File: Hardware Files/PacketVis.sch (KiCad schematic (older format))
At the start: 36 parts, among them J1 USB_B_Micro, J2 Conn_01x04, SW1 SW_Push_Dual, SW2 SW_SPST, SW3 SW_SPST, U1 3.3V 1A, U2 74HC595, U3 ESP-WROOM-02D

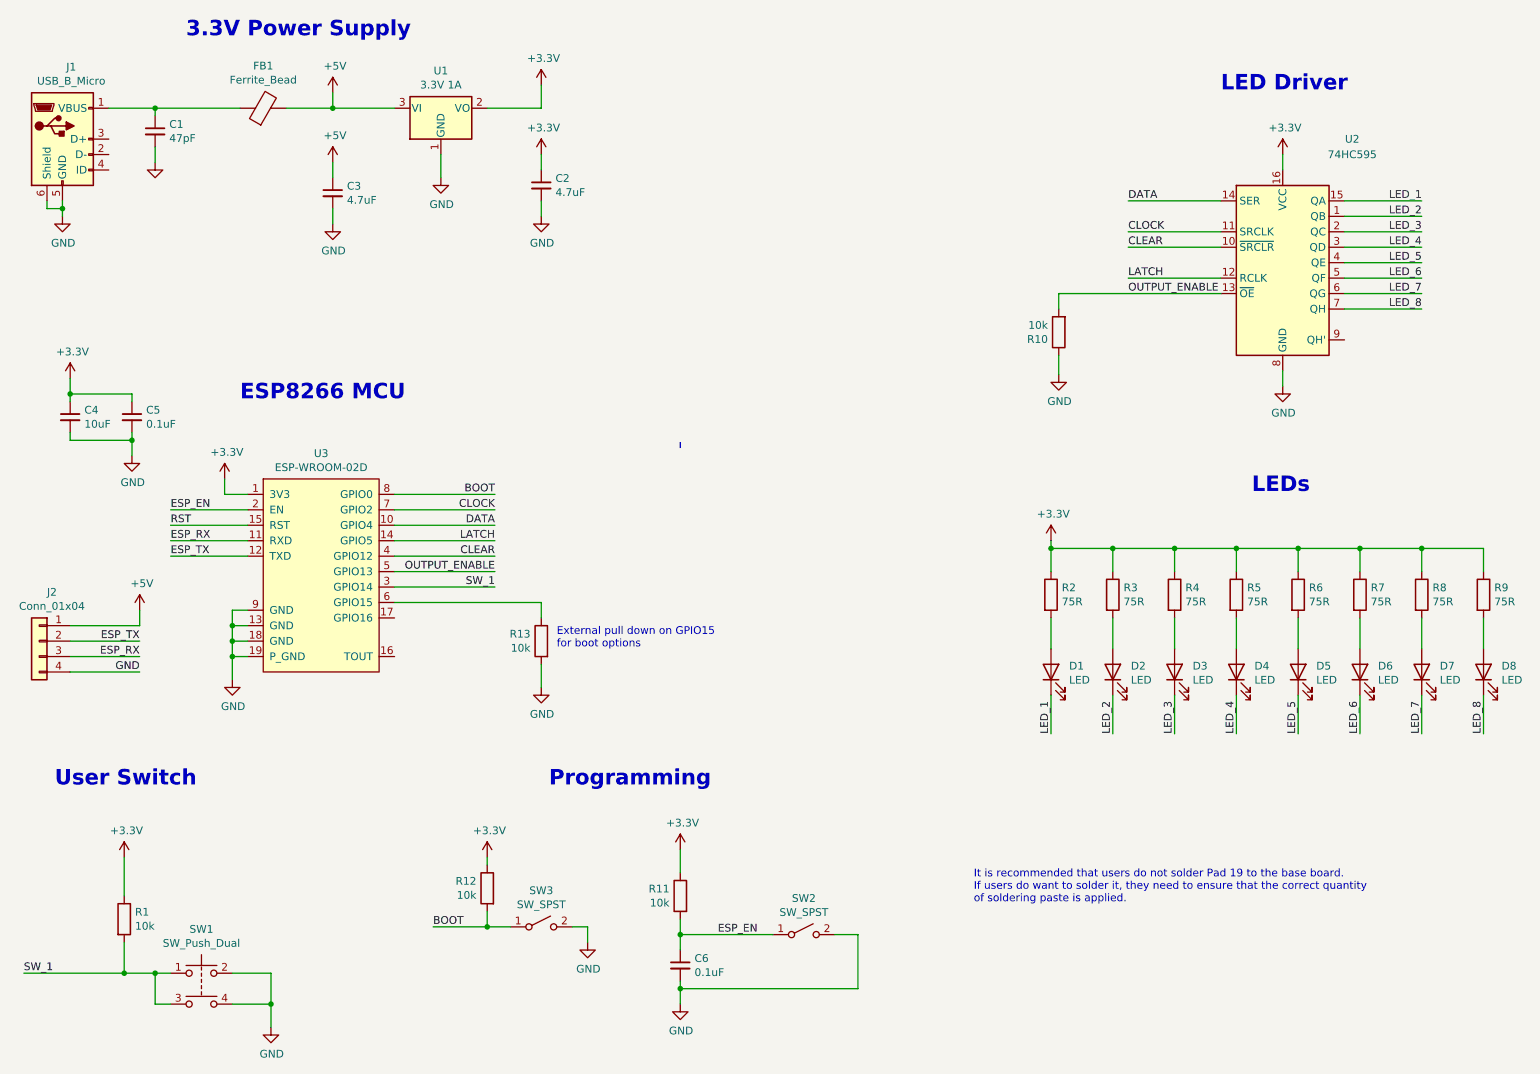
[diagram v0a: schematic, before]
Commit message: Change LEDs to source current from shift register, unroute most tracks
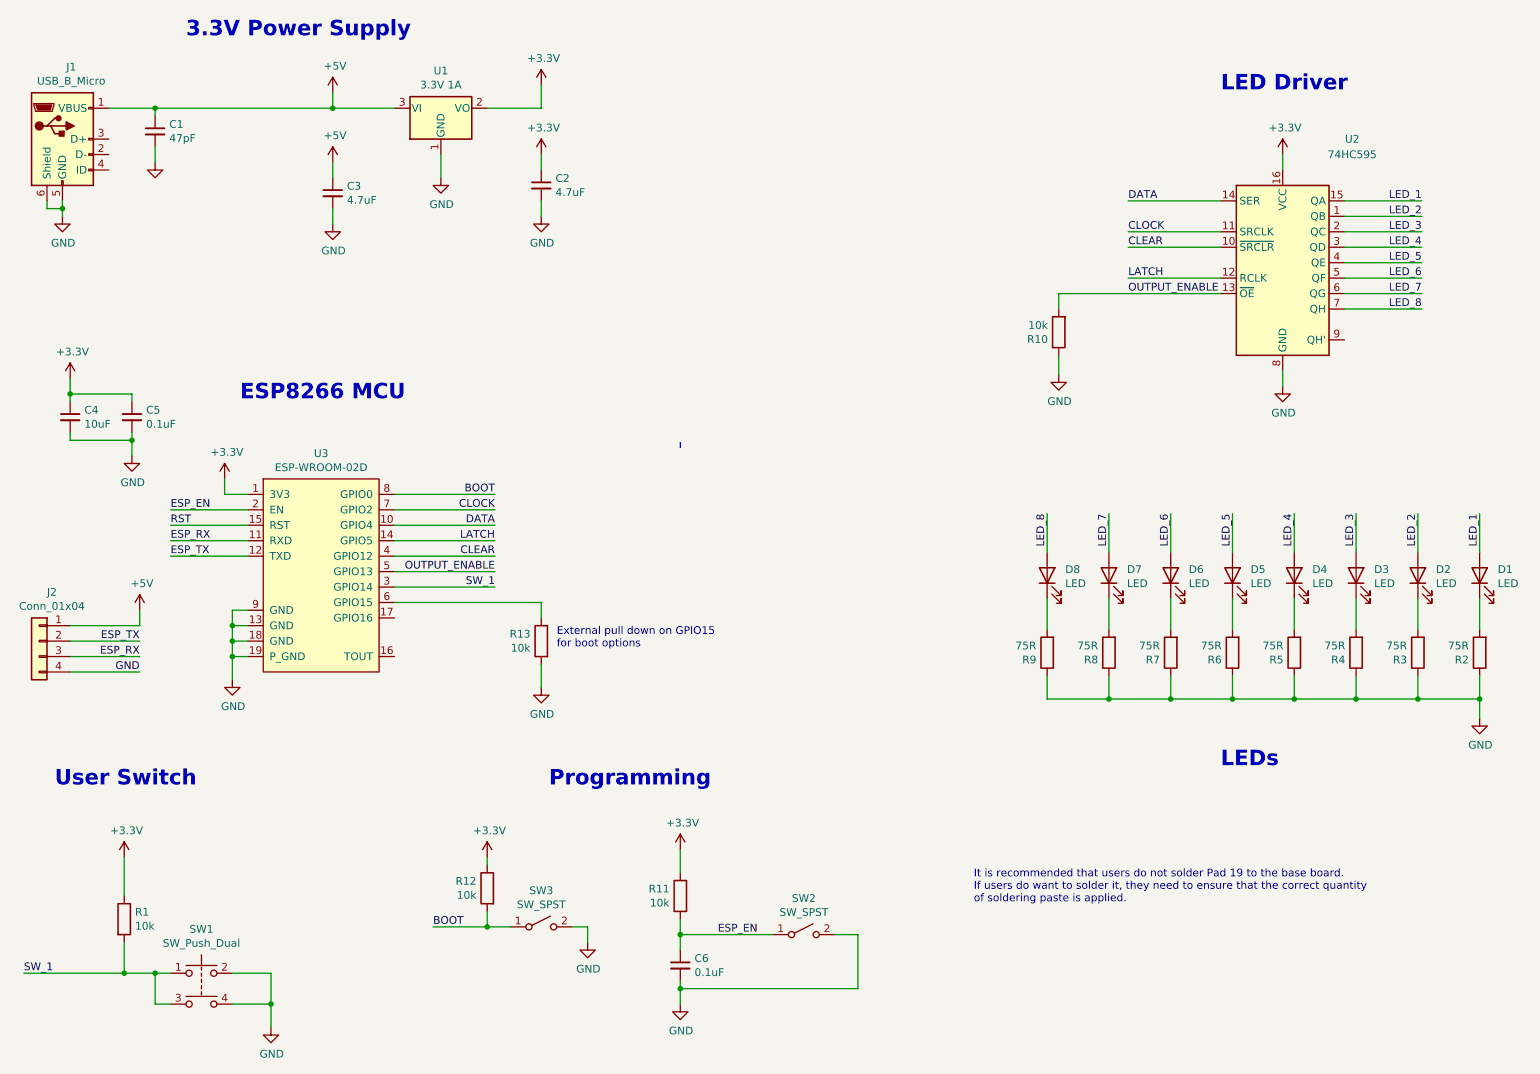
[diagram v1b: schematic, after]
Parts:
- removed FB1: Ferrite_Bead, Inductor_SMD:L_0805_2012Metric, symbol Device:Ferrite_Bead
- U2: footprint PacketVis_Footprints:SOIC-16 -> Package_SO:SOIC-16_3.9x9.9mm_P1.27mm
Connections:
- net +3V3: no longer R2.1, R3.1, R4.1, R5.1, R6.1, R7.1, R8.1, R9.1
- net +5V: now also C1.1, J1.1 (VBUS)
- net GND: now also R2.1, R3.1, R4.1, R5.1, R6.1, R7.1, R8.1, R9.1
- net LED_1: now also D1.2 (A); no longer D1.1 (K)
- net LED_2: now also D2.2 (A); no longer D2.1 (K)
- net LED_3: now also D3.2 (A); no longer D3.1 (K)
- net LED_4: now also D4.2 (A); no longer D4.1 (K)
- net LED_5: now also D5.2 (A); no longer D5.1 (K)
- net LED_6: now also D6.2 (A); no longer D6.1 (K)
- net LED_7: now also D7.2 (A); no longer D7.1 (K)
- net LED_8: now also D8.2 (A); no longer D8.1 (K)
- net at R2.2: now also D1.1 (K); no longer D1.2 (A)
- net at R3.2: now also D2.1 (K); no longer D2.2 (A)
- net at R4.2: now also D3.1 (K); no longer D3.2 (A)
- net at R5.2: now also D4.1 (K); no longer D4.2 (A)
- net at R6.2: now also D5.1 (K); no longer D5.2 (A)
- net at R7.2: now also D6.1 (K); no longer D6.2 (A)
- net at R8.2: now also D7.1 (K); no longer D7.2 (A)
- net at R9.2: now also D8.1 (K); no longer D8.2 (A)
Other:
- moved on the sheet: D1, D2, D3, D4, D5, D6, D7, D8, R2, R3, R4, R5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

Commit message: Update Routing
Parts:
- removed C1: 47pF, Capacitor_SMD:C_0805_2012Metric, symbol Device:C_Small
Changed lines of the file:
@@
 $EndComp
-$Comp
-L Device:C_Small C1
-U 1 1 5E17E0E8
-P 1700 1350
-F 0 "C1" H 1792 1396 50  0000 L CNN
-F 1 "47pF" H 1792 1305 50  0000 L CNN
-F 2 "Capacitor_SMD:C_0805_2012Metric" H 1700 1350 50  0001 C CNN
-F 3 "~" H 1700 1350 50  0001 C CNN
-F 4 "CC0805JRNPO9BN470" H 1700 1350 50  0001 C CNN "Manufacturer PN"
-	1    1700 1350
-	1    0    0    -1
-$EndComp
-Wire Wire Line
-	1700 1250 1700 1200
-Connection ~ 1700 1200
-$Comp
-L power:GND #PWR04
-U 1 1 5E19F43B
-P 1700 1550
-F 0 "#PWR04" H 1700 1300 50  0001 C CNN
-F 1 "GND" H 1705 1377 50  0001 C CNN
-F 2 "" H 1700 1550 50  0001 C CNN
-F 3 "" H 1700 1550 50  0001 C CNN
-	1    1700 1550
-	1    0    0    -1
-$EndComp
-Wire Wire Line
-	1700 1450 1700 1550
 $Comp
 L Switch:SW_SPST SW2
@@
 Text Notes 7000 6350 0    50   ~ 0
 It is recommended that users do not solder Pad 19 to the base board. \nIf users do want to solder it, they need to ensure that the correct quantity \nof soldering paste is applied.
-Wire Wire Line
-	1400 1200 1700 1200
 Wire Wire Line
 	5100 6900 5100 7000
@@
 	10275 5025 10275 5150
 Wire Wire Line
-	1700 1200 2850 1200
+	1400 1200 2850 1200
 $EndSCHEMATC
